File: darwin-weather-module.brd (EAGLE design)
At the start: 95 x 25 mm, 24 parts, among them J1 2X6-HEADERS, J2 95501-6889VERT, U2 ATSAMD09, U3 M24C02-WMN6TP, U4 PCA9615

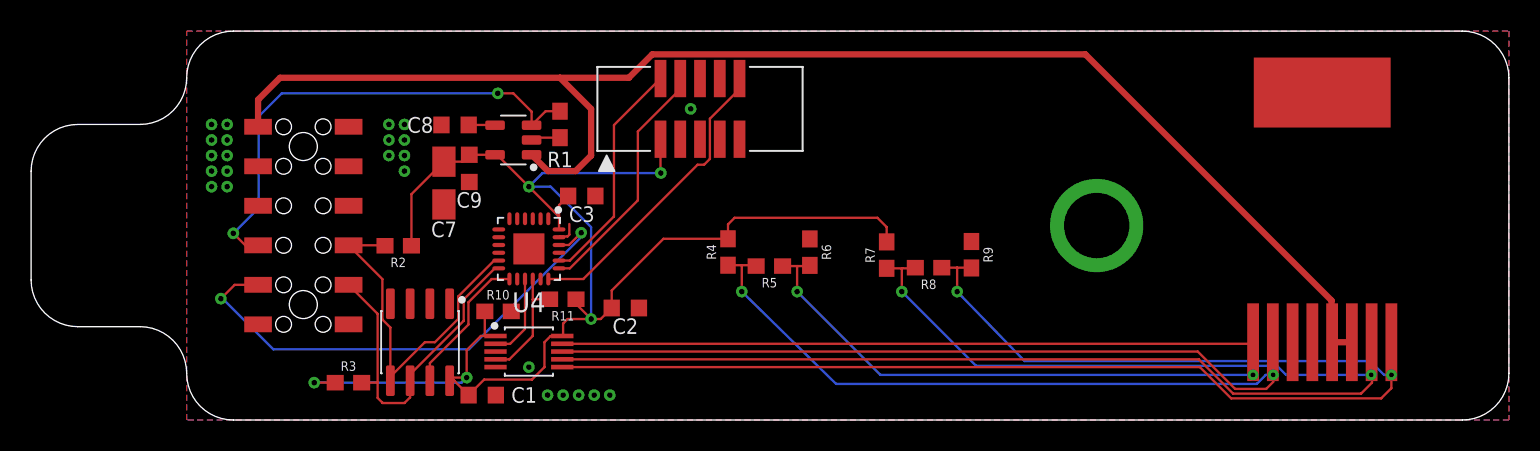
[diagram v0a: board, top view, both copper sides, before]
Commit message: Changed Power Architecture for Sensor/Module synchronization. TA3.
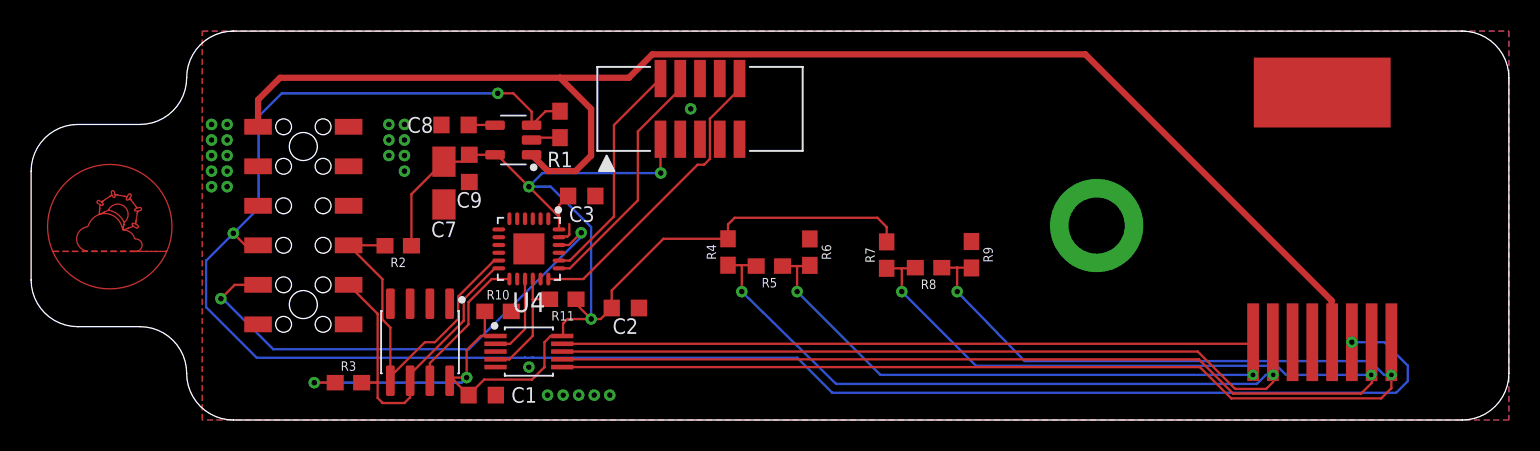
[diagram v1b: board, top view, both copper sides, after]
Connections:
- net ENABLE: now also J2.3
- net UNREG: no longer J2.3
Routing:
- net ENABLE: track 31.8 -> 122.4 mm, vias 2 -> 3
- net UNREG: track 93.0 -> 91.7 mm
- added copper zone on layer 1, net GND1
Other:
- board text added: "THIS SIDE DOWN"

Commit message: New module footprint, icon, and relocated programming header.
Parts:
- moved X1 22.0 mm to (55.0, 19.5)
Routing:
- net RESET: track 19.5 -> 39.9 mm
- net SWCLK: track 15.8 -> 35.1 mm
- net SWDIO: track 14.8 -> 33.6 mm
- net 3V3: track 96.7 -> 95.7 mm, vias 5 -> 4
- net GND: vias 24 -> 25

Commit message: Migrated programming header to Tag-Connect.
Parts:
- removed X1: (no value), microbuilder:2X05_1.27MM_BOX_NOPOSTS
- added J3: TAG-CONNECT, Conservify:TC2030-IDC
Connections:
- removed net KEY: X1.7
- removed net SWO: X1.6
- removed net TDI: X1.8
- net 3V3: now also J3.VCC; no longer X1.1
- net GND: now also J3.GND; no longer X1.3, X1.5, X1.9
- net RESET: now also J3.NRESET; no longer X1.10
- net SWCLK: now also J3.SWCLK/TCK; no longer X1.4
- net SWDIO: now also J3.SWDIO/TMS; no longer X1.2
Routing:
- net 3V3: track 95.7 -> 115.0 mm, vias 4 -> 5
- net RESET: track 39.9 -> 24.1 mm
- net SWDIO: track 33.6 -> 21.0 mm
- net SWCLK: track 35.1 -> 29.0 mm, vias 0 -> 2
- net GND: track 3.30 -> 6.61 mm
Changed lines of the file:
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@@
 <?xml version="1.0" encoding="utf-8"?>
 <!DOCTYPE eagle SYSTEM "eagle.dtd">
-<eagle version="9.5.0">
+<eagle version="9.6.1">
 <drawing>
 <settings>
@@
 </layers>
 <board>
-<fusionsync huburn="a.cGVyc29uYWw6dWUyZGRkM2Mx" projecturn="a.cGVyc29uYWw6dWUyZGRkM2MxIzIwMTgwNTA0MTMwNDQ3NTc2" f3durn="urn:adsk.wipprod:dm.lineage:CBy5YJjYQJG541fhUPEFrg" pcbguid="3b7475b6-4468-4637-a01f-e463c0ad595c" lastpulledtime="" lastsyncedchangeguid="9d5eeb8a-007b-4141-6704-704761fe4ee1"/>
+<fusionsync huburn="a.cGVyc29uYWw6dWUyZGRkM2Mx" projecturn="a.cGVyc29uYWw6dWUyZGRkM2MxIzIwMTgwNTA0MTMwNDQ3NTc2" f3durn="urn:adsk.wipprod:dm.lineage:CBy5YJjYQJG541fhUPEFrg" pcbguid="3b7475b6-4468-4637-a01f-e463c0ad595c" lastpulledtime="" lastsyncedchangeguid="9d5eeb8a-007b-4141-6704-704761fe4ee1" latestrevisionid="" lastsyncedrevisionid="" lastboardhashguid="" lastpushedtime="" linktopcb3d="%12"/>
 <plain>
 <wire x1="82" y1="0" x2="85" y2="3" width="0" layer="20" curve="90"/>
@@
 <param name="mdViaViaSameLayer" value="6mil"/>
 <param name="mnLayersViaInSmd" value="2"/>
-<param name="mdCopperDimension" value="40mil"/>
+<param name="mdCopperDimension" value="6mil"/>
 <param name="mdDrill" value="6mil"/>
 <param name="mdSmdStop" value="0mil"/>
@@
 <attribute name="PROD_ID" value="RES-07828" x="29" y="-4" size="1.778" layer="27" rot="R90" display="off"/>
 </element>
-<element name="X1" library="microbuilder" package="2X05_1.27MM_BOX_NOPOSTS" value="" x="55" y="19.5" smashed="yes">
-<attribute name="VALUE" x="48.9" y="17.1" size="0.4064" layer="27" ratio="10"/>
-</element>
 <element name="U3" library="Conservify" library_urn="urn:adsk.eagle:library:11839183" package="SOIC127P600X175-8" package3d_urn="urn:adsk.eagle:package:12022475/1" value="M24C02-WMN6TP" x="15" y="5" smashed="yes" rot="R270"/>
 <element name="J2" library="Conservify" library_urn="urn:adsk.eagle:library:11839183" package="85513-5009" package3d_urn="urn:adsk.eagle:package:12024212/2" value="95501-6889VERT" x="73" y="5" smashed="yes"/>
@@
 <attribute name="VALUE" x="24.181" y="8.526" size="0.6096" layer="27" font="vector" ratio="20" rot="R180" align="top-center"/>
 </element>
+<element name="J3" library="Conservify" library_urn="urn:adsk.eagle:library:11839183" package="TC2030-IDC" package3d_urn="urn:adsk.eagle:package:16969550/1" value="TAG-CONNECT" x="39.769" y="18.478" smashed="yes"/>
 </elements>
 <signals>
@@
 <contactref element="C7" pad="-"/>
 <contactref element="R1" pad="1"/>
-<contactref element="X1" pad="3"/>
-<contactref element="X1" pad="5"/>
-<contactref element="X1" pad="9"/>
 <contactref element="U2" pad="23"/>
 <wire x1="22.175" y1="18" x2="22.325" y2="18.15" width="0.1524" layer="1"/>
@@
 <via x="27.6756" y="14.3866" extent="1-16" drill="0.35"/>
 <via x="30.4696" y="7.2238" extent="1-16" drill="0.35"/>
+<contactref element="J3" pad="GND"/>
+<wire x1="43.579" y1="17.843" x2="43.815" y2="17.607" width="0.1524" layer="1"/>
+<wire x1="43.815" y1="17.607" x2="43.815" y2="17.399" width="0.1524" layer="1"/>
+<wire x1="43.815" y1="17.399" x2="45.214" y2="16" width="0.1524" layer="1"/>
+<wire x1="45.214" y1="16" x2="46" y2="16" width="0.1524" layer="1"/>
 </signal>
 <signal name="3V3">
@@
 <contactref element="U$4" pad="5"/>
 <contactref element="C9" pad="1"/>
-<contactref element="X1" pad="1"/>
 <contactref element="U2" pad="24"/>
 <wire x1="19.825" y1="17.05" x2="18.169" y2="17.05" width="0.1524" layer="1"/>
@@
 <wire x1="45" y1="11.45" x2="45.55" y2="12" width="0.1524" layer="1"/>
 <wire x1="45.55" y1="12" x2="46" y2="12" width="0.1524" layer="1"/>
-<wire x1="51.55" y1="17.55" x2="52.46" y2="17.55" width="0.1524" layer="1"/>
 <wire x1="46" y1="12" x2="51.55" y2="17.55" width="0.1524" layer="1"/>
+<contactref element="J3" pad="VCC"/>
+<wire x1="41.039" y1="17.843" x2="40.595" y2="17.399" width="0.1524" layer="1"/>
+<wire x1="38.399" y1="17.399" x2="38" y2="17" width="0.1524" layer="1"/>
+<via x="38" y="17" extent="1-16" drill="0.35"/>
+<wire x1="38" y1="17" x2="36" y2="15" width="0.1524" layer="16"/>
+<wire x1="36" y1="15" x2="22" y2="15" width="0.1524" layer="16"/>
+<wire x1="40.595" y1="17.399" x2="38.399" y2="17.399" width="0.1524" layer="1"/>
 </signal>
 <signal name="N$6">
@@
 </signal>
 <signal name="SWCLK">
-<contactref element="X1" pad="4"/>
 <contactref element="U2" pad="19"/>
-<wire x1="53.73" y1="20.63" x2="53.73" y2="21.45" width="0.1524" layer="1"/>
-<wire x1="52.4048" y1="19.3048" x2="53.73" y2="20.63" width="0.1524" layer="1"/>
-<wire x1="25.6810625" y1="9.75" x2="35.2358625" y2="19.3048" width="0.1524" layer="1"/>
-<wire x1="35.2358625" y1="19.3048" x2="52.4048" y2="19.3048" width="0.1524" layer="1"/>
-<wire x1="23.9373" y1="9.75" x2="25.6810625" y2="9.75" width="0.1524" layer="1"/>
+<wire x1="25.6810625" y1="9.75" x2="23.9373" y2="9.75" width="0.1524" layer="1"/>
+<contactref element="J3" pad="SWCLK/TCK"/>
+<wire x1="42.309" y1="18.986" x2="41.402" y2="19.893" width="0.1524" layer="1"/>
+<via x="41.402" y="22.479" extent="1-16" drill="0.35"/>
+<wire x1="41.402" y1="22.479" x2="41.402" y2="18.402" width="0.1524" layer="16"/>
+<wire x1="32.779" y1="9.779" x2="27.178" y2="9.779" width="0.1524" layer="16"/>
+<via x="27.178" y="9.779" extent="1-16" drill="0.35"/>
+<wire x1="27.178" y1="9.779" x2="25.7100625" y2="9.779" width="0.1524" layer="1"/>
+<wire x1="25.7100625" y1="9.779" x2="25.6810625" y2="9.75" width="0.1524" layer="1"/>
+<wire x1="41.402" y1="19.893" x2="41.402" y2="22.479" width="0.1524" layer="1"/>
+<wire x1="41.402" y1="18.402" x2="32.779" y2="9.779" width="0.1524" layer="16"/>
 </signal>
 <signal name="SWDIO">
-<contactref element="X1" pad="2"/>
 <contactref element="U2" pad="20"/>
-<wire x1="52.46" y1="20.63" x2="52.46" y2="21.45" width="0.1524" layer="1"/>
-<wire x1="51.4396" y1="19.6096" x2="52.46" y2="20.63" width="0.1524" layer="1"/>
-<wire x1="25.75" y1="10.25" x2="35.1096" y2="19.6096" width="0.1524" layer="1"/>
-<wire x1="35.1096" y1="19.6096" x2="51.4396" y2="19.6096" width="0.1524" layer="1"/>
-<wire x1="23.9373" y1="10.25" x2="25.75" y2="10.25" width="0.1524" layer="1"/>
+<wire x1="25.75" y1="10.25" x2="23.9373" y2="10.25" width="0.1524" layer="1"/>
+<contactref element="J3" pad="SWDIO/TMS"/>
+<wire x1="41.039" y1="18.986" x2="40.704" y2="18.986" width="0.1524" layer="1"/>
+<wire x1="40.704" y1="18.986" x2="40.386" y2="19.304" width="0.1524" layer="1"/>
+<wire x1="40.386" y1="19.304" x2="34.804" y2="19.304" width="0.1524" layer="1"/>
+<wire x1="34.804" y1="19.304" x2="25.75" y2="10.25" width="0.1524" layer="1"/>
 </signal>
 <signal name="RESET">
-<contactref element="X1" pad="10"/>
 <contactref element="U2" pad="18"/>
-<wire x1="57.54" y1="20.63" x2="57.54" y2="21.45" width="0.1524" layer="1"/>
-<wire x1="55.91" y1="19" x2="57.54" y2="20.63" width="0.1524" layer="1"/>
-<wire x1="25.424825" y1="9.0627" x2="35.362125" y2="19" width="0.1524" layer="1"/>
-<wire x1="35.362125" y1="19" x2="55.91" y2="19" width="0.1524" layer="1"/>
-<wire x1="23.25" y1="9.0627" x2="25.424825" y2="9.0627" width="0.1524" layer="1"/>
-</signal>
-<signal name="KEY">
-<contactref element="X1" pad="7"/>
-</signal>
-<signal name="SWO">
-<contactref element="X1" pad="6"/>
-</signal>
-<signal name="TDI">
-<contactref element="X1" pad="8"/>
+<contactref element="J3" pad="NRESET"/>
+<wire x1="42.309" y1="17.843" x2="41.402" y2="16.936" width="0.1524" layer="1"/>
+<wire x1="41.402" y1="16.936" x2="41.402" y2="14.605" width="0.1524" layer="1"/>
+<wire x1="41.402" y1="14.605" x2="40.162" y2="13.365" width="0.1524" layer="1"/>
+<wire x1="27.63164375" y1="9.0627" x2="23.25" y2="9.0627" width="0.1524" layer="1"/>
+<wire x1="40.162" y1="13.365" x2="31.93394375" y2="13.365" width="0.1524" layer="1"/>
+<wire x1="31.93394375" y1="13.365" x2="27.63164375" y2="9.0627" width="0.1524" layer="1"/>
 </signal>
 <signal name="SDA">
